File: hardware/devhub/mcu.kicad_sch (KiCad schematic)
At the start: 19 parts, among them J4 SWD, J9 UART debug, U3 STM32G0B1RET6

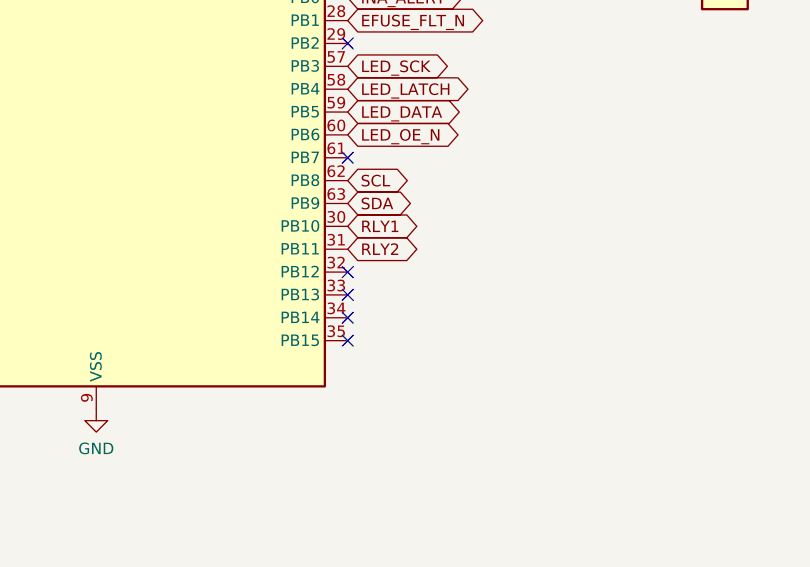
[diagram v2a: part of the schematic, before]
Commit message: SMAJ20A input TVS, no TVS on ports (D24, D25); relay push buttons (D26)
- The SMAJ5.0A already conducted at ~6.4 V and would burn with a 12-20 V
  supply before the eFuse trips; the SMAJ20A lets the eFuse do its job.
  No TVS on ports: it does not help against a sustained back-fed voltage.
  Two LEDs per port confirmed.
- SW1/SW2 on PB12/PB13 toggle the relays; new requirement RF-17 on panel
  buttons, RELAY_CHANGED event in the protocol.

Targeted schematic changes, connectivity otherwise unchanged, ERC clean.
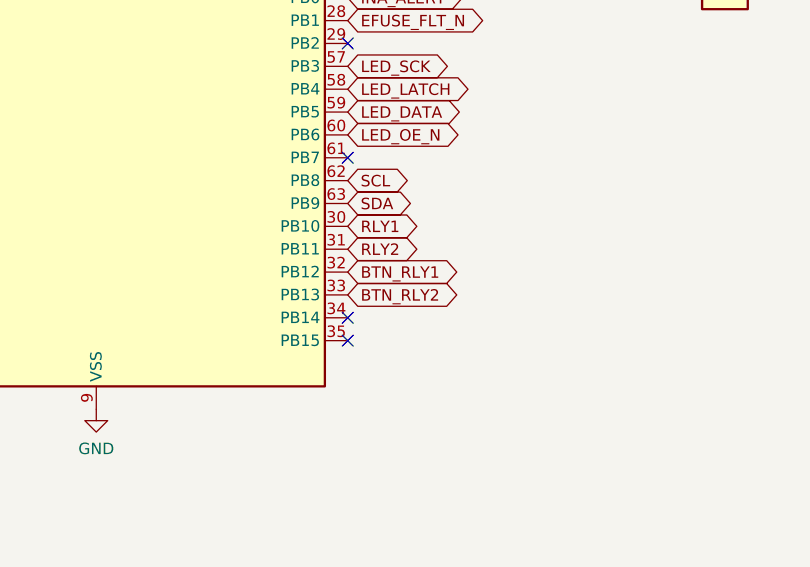
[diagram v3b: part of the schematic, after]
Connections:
- net BTN_RLY1: now reaches U3.32 (PB12)
- net BTN_RLY2: now reaches U3.33 (PB13)
- no-connect marks 15 -> 13
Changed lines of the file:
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@@
 		(at 266.7 154.94)
 	)
-	(no_connect
-		(at 231.14 190.5)
+	(global_label "BTN_RLY1"
+		(shape bidirectional)
+		(at 231.14 190.5 0)
+		(fields_autoplaced yes)
+		(effects
+			(font
+				(size 1.27 1.27)
+			)
+			(justify left)
+		)
+		(property "Intersheetrefs" "${INTERSHEET_REFS}"
+			(at 231.14 190.5 0)
+			(hide yes)
+			(show_name no)
+			(do_not_autoplace no)
+			(effects
+				(font
+					(size 1.27 1.27)
+				)
+			)
+		)
 	)
 	(no_connect
@@
 		(at 231.14 134.62)
 	)
-	(no_connect
-		(at 231.14 193.04)
+	(global_label "BTN_RLY2"
+		(shape bidirectional)
+		(at 231.14 193.04 0)
+		(fields_autoplaced yes)
+		(effects
+			(font
+				(size 1.27 1.27)
+			)
+			(justify left)
+		)
+		(property "Intersheetrefs" "${INTERSHEET_REFS}"
+			(at 231.14 193.04 0)
+			(hide yes)
+			(show_name no)
+			(do_not_autoplace no)
+			(effects
+				(font
+					(size 1.27 1.27)
+				)
+			)
+		)
 	)
 	(no_connect

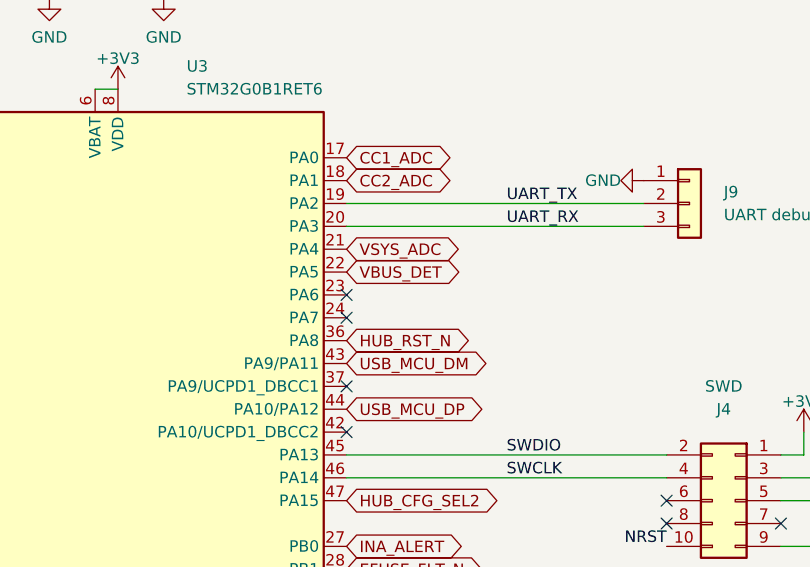
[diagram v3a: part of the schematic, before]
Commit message: Review 02, R02-05: drop RF-16, logic powered from the supply only (D32)
Removed D3; VBUS_DET and VSYS_ADC moved to 5 V tolerant pins (PA6, PA7).
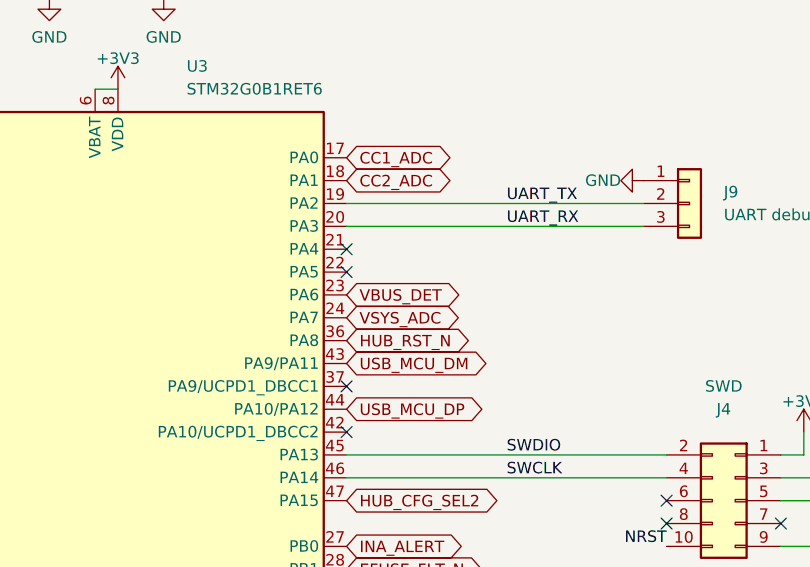
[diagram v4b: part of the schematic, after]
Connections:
- net VBUS_DET: now also U3.23 (PA6); no longer U3.22 (PA5)
- net VSYS_ADC: now also U3.24 (PA7); no longer U3.21 (PA4)
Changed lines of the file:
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@@
 	)
 	(no_connect
-		(at 231.14 134.62)
+		(at 231.14 129.54)
 	)
 	(global_label "BTN_RLY2"
@@
 	)
 	(no_connect
-		(at 231.14 132.08)
+		(at 231.14 127)
 	)
 	(no_connect
@@
 	(global_label "VSYS_ADC"
 		(shape bidirectional)
-		(at 231.14 127 0)
-		(fields_autoplaced yes)
-		(effects
-			(font
-				(size 1.27 1.27)
-			)
-			(justify left)
-		)
-		(property "Intersheetrefs" "${INTERSHEET_REFS}"
-			(at 231.14 127 0)
+		(at 231.14 134.62 0)
+		(fields_autoplaced yes)
+		(effects
+			(font
+				(size 1.27 1.27)
+			)
+			(justify left)
+		)
+		(property "Intersheetrefs" "${INTERSHEET_REFS}"
+			(at 231.14 134.62 0)
 			(hide yes)
 			(show_name no)
@@
 	(global_label "VBUS_DET"
 		(shape bidirectional)
-		(at 231.14 129.54 0)
-		(fields_autoplaced yes)
-		(effects
-			(font
-				(size 1.27 1.27)
-			)
-			(justify left)
-		)
-		(property "Intersheetrefs" "${INTERSHEET_REFS}"
-			(at 231.14 129.54 0)
-			(hide yes)
-			(show_name no)
+		(at 231.14 132.08 0)
+		(fields_autoplaced yes)
+		(effects
+			(font
+				(size 1.27 1.27)
+			)
+			(justify left)
+		)
+		(property "Intersheetrefs" "${INTERSHEET_REFS}"
+			(at 231.14 132.08 0)
+			(hide yes)
+			(show_name no)

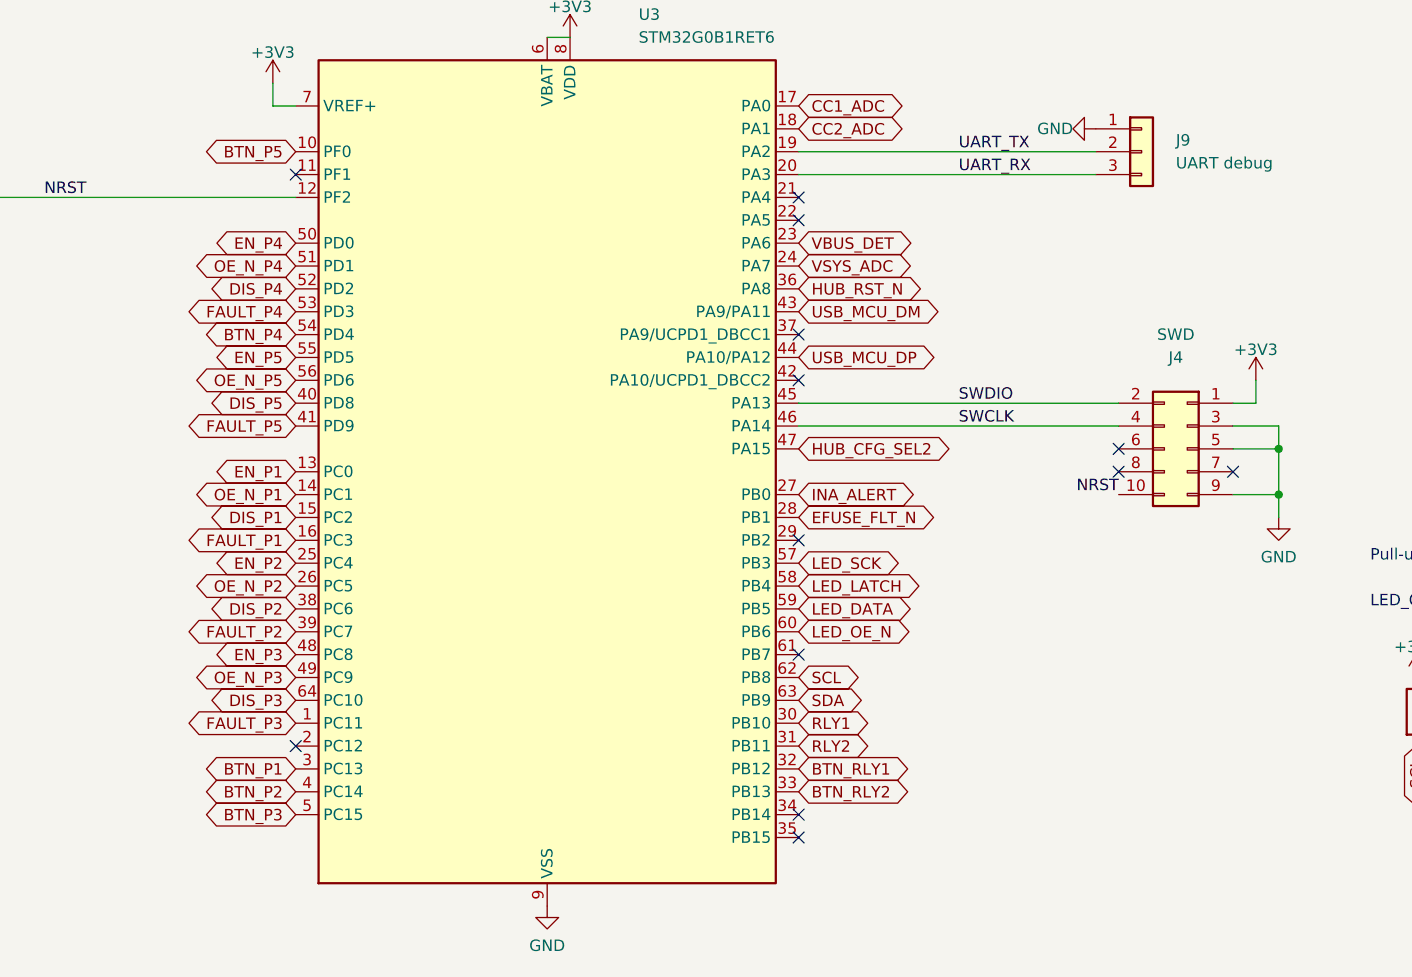
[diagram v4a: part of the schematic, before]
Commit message: Review 02, R02-07: MCU pins compatible with UCPD and the ST bootloader (D34)
Hub reset moved to PF1, pull-downs on the DBCC pins.
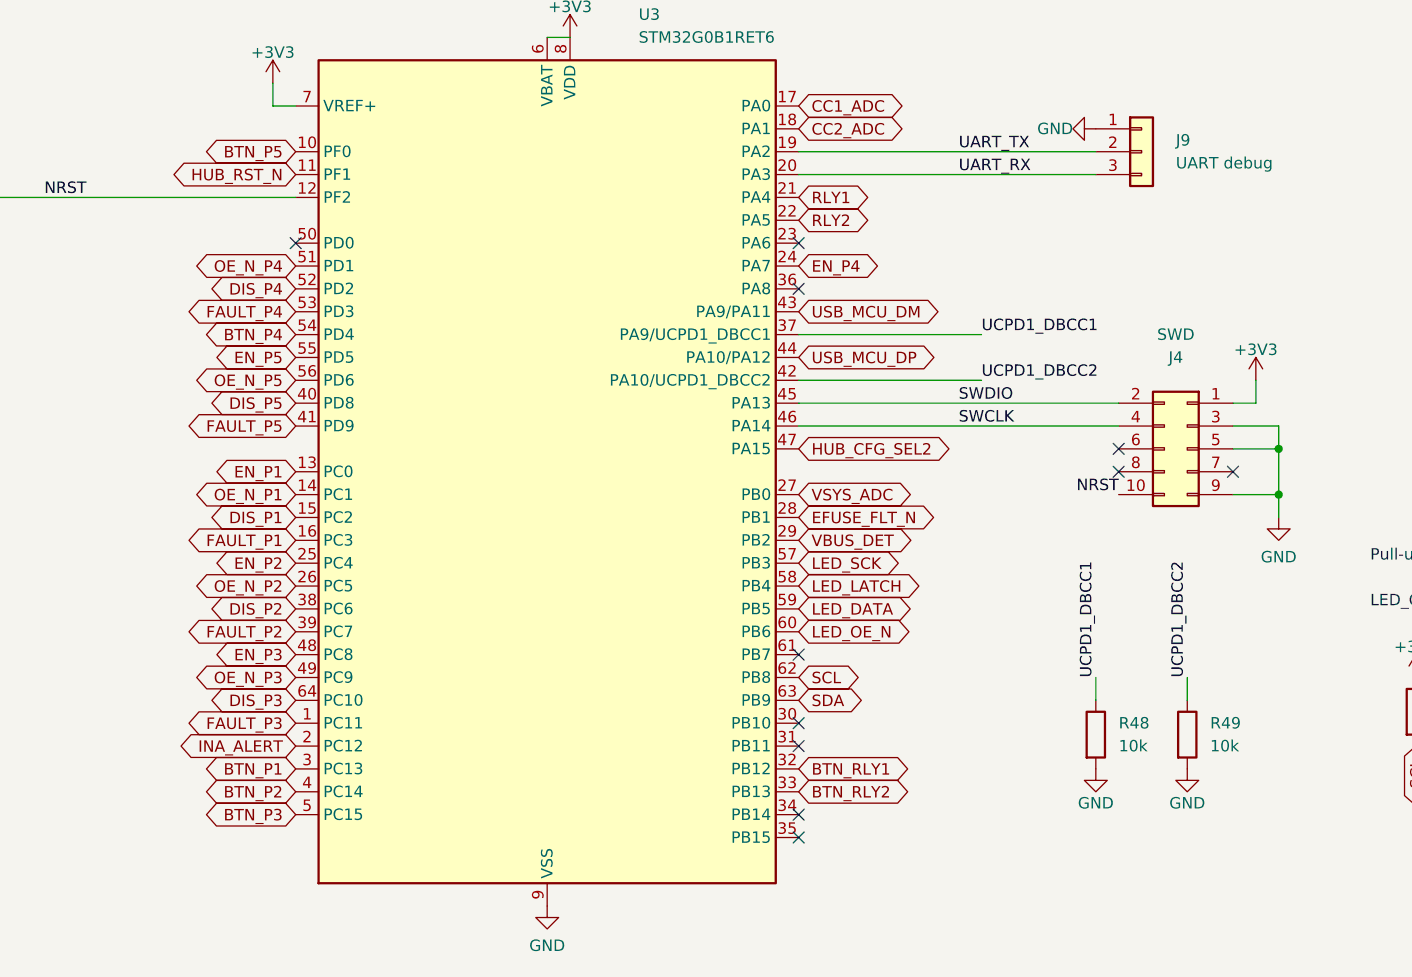
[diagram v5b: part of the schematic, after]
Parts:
- added R48, R49: 10k, Resistor_SMD:R_0603_1608Metric, symbol Device:R
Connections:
- net EN_P4: now also U3.24 (PA7); no longer U3.50 (PD0)
- net GND: now also R48.2, R49.2
- net HUB_RST_N: now also U3.11 (PF1); no longer U3.36 (PA8)
- net INA_ALERT: now also U3.2 (PC12); no longer U3.27 (PB0)
- net RLY1: now also U3.21 (PA4); no longer U3.30 (PB10)
- net RLY2: now also U3.22 (PA5); no longer U3.31 (PB11)
- net VBUS_DET: now also U3.29 (PB2); no longer U3.23 (PA6)
- net VSYS_ADC: now also U3.27 (PB0); no longer U3.24 (PA7)
- net UCPD1_DBCC1: now reaches U3.37 (PA9/UCPD1_DBCC1)
- net UCPD1_DBCC1: now also R48.1
- net UCPD1_DBCC2: now reaches U3.42 (PA10/UCPD1_DBCC2)
- net UCPD1_DBCC2: now also R49.1
- no-connect marks 13 -> 11
